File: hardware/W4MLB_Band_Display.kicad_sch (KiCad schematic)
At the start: 23 parts, among them J1 SSW-115-01-G-S, J2 SSW-115-01-G-S, J3 SSQ-108-01-T-D-LL, J4 SAMTEC-TST-108-01-X-D, J5 EJ503B, J6 4DB-P108-02, J7 PJRAN1X1U01X, J8 PJRAN1X1U01X, J9 Conn_01x09, Q1 MMBT2222A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

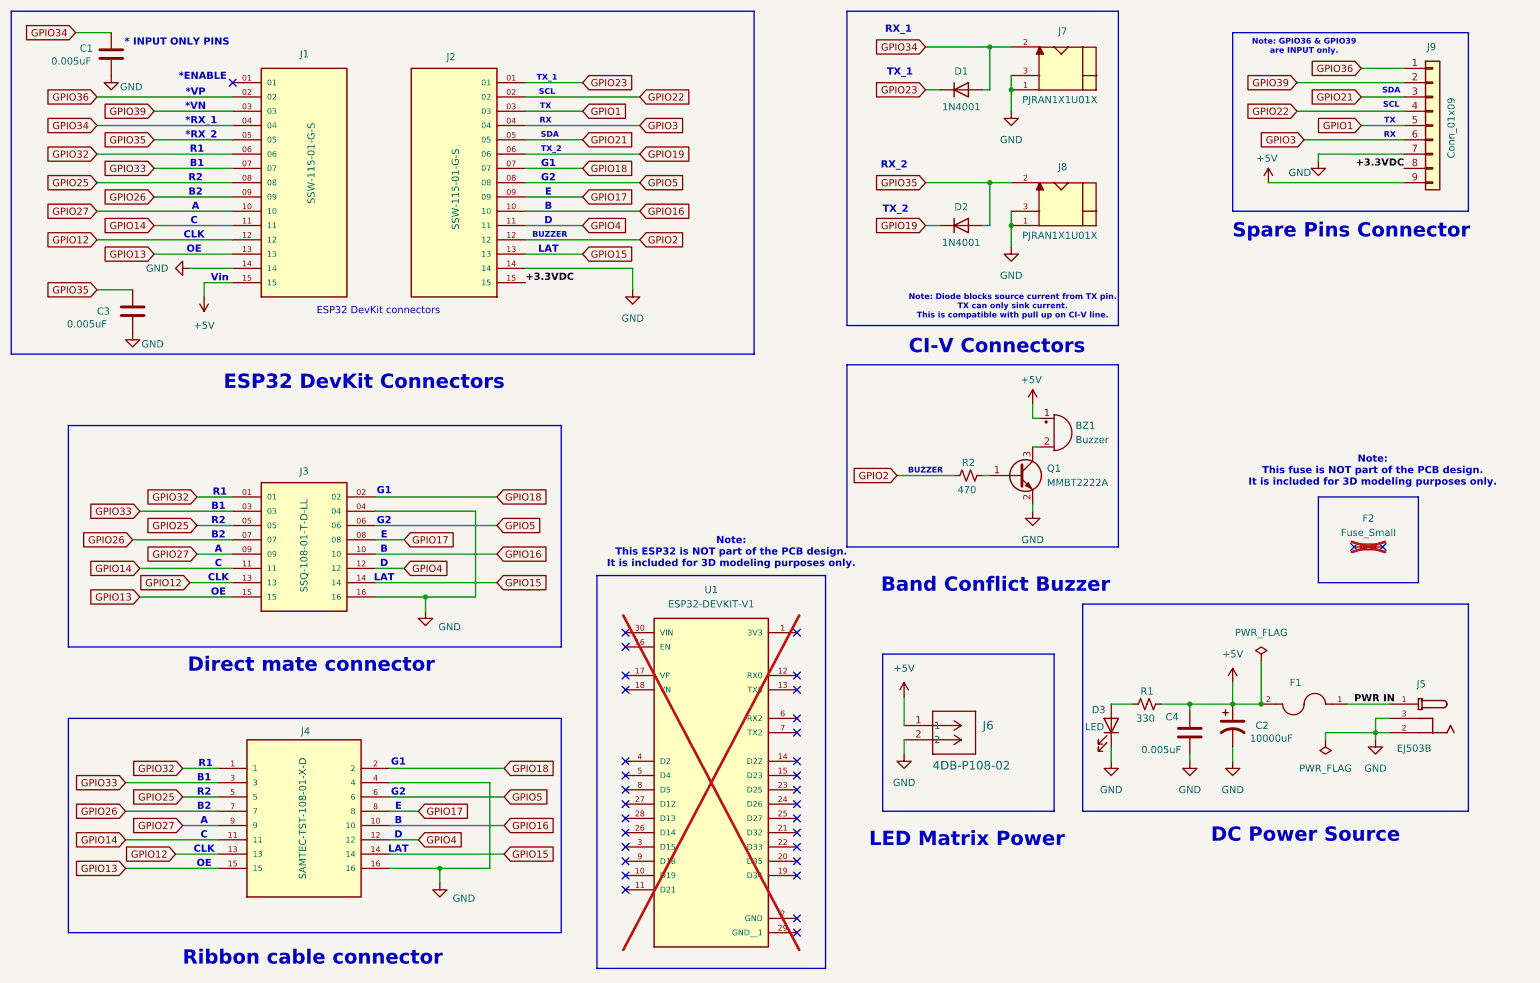
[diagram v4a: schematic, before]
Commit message: Update RF decoupling caps to 4.7nF
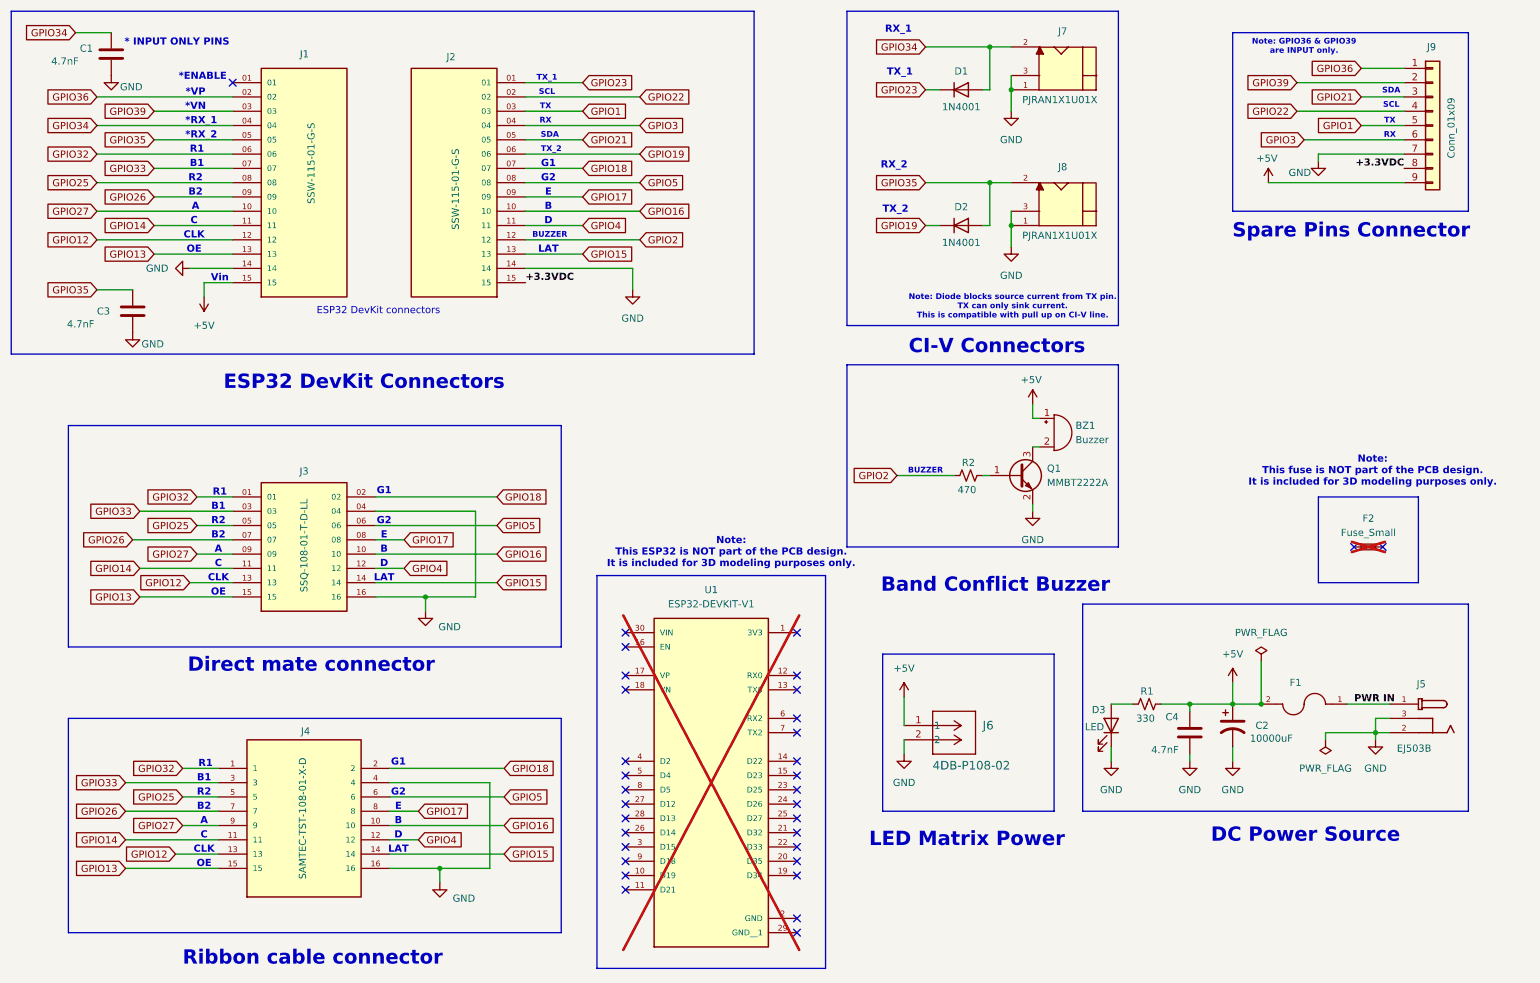
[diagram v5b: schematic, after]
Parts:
- C1, C3, C4: value 0.005uF -> 4.7nF
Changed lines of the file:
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@@
 			)
 		)
-		(property "Value" "0.005uF"
-			(at 219.964 145.288 0)
+		(property "Value" "4.7nF"
+			(at 221.742 145.288 0)
 			(effects
 				(font
@@
 			)
 		)
-		(property "Value" "0.005uF"
+		(property "Value" "4.7nF"
 			(at 28.956 69.596 0)
 			(effects
@@
 			)
 		)
-		(property "Value" "0.005uF"
+		(property "Value" "4.7nF"
 			(at 26.162 22.86 0)
 			(effects
